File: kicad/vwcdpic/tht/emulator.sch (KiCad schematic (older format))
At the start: 33 parts, among them P1 CONN_9, P2 CONN_3, Q1 IRF7343PBF, U1 PIC12F629, U2 78L05, U3 TL072

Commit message: tht separated board for emulator, separated board for audio
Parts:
- removed C6, C7: 10m, symbol C
- removed C8: 47m, symbol C
- removed Q1: IRF7343PBF, SO8, symbol IRF7343PBF
- removed R10, R11: 10k, symbol R
- removed R18: 10, symbol R
- added C10, C11, C12, C13, C14, C16, C18, C6: 100m, symbol CAPAPOL
- added C15, C17: 100n, symbol C
- added C7, C8: 10m, symbol CAPAPOL
- added P3: Aout, symbol CONN_4
- added R19, R20: 100, symbol R
- added RV1, RV2: 100k, symbol POT
- added U4: TL071, symbol TL071
- C4: value C -> 1m
- C5: value 2m2 -> 100n
- C9: value 47m -> 100n
- P1: value CONN_9 -> digi; symbol CONN_9 -> CONN_7
- P2: value CONN_3 -> Ain
- R14, R15: value 330k -> 2k2
- R16, R17: value 7M5 -> 22k
- R2: value 1M -> 22k
- R3: value 1k -> 22k
- R4: value 1k5 -> 10
- R8, R9: value 10k -> 100k
- U2: footprint (none) -> to92
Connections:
- net +12V: now also R4.2, C17.1, C18.1, P3.4 (P4); no longer P1.4 (P4), R3.2, R8.2, U3.8 (V+), U3.8 (V+)
- net AGND: now also C5.2, C9.2, R3.2, R8.1, R9.1, U3.4 (V-), U3.4 (V-), C10.2, C11.2, C12.2, C15.2, C16.2, C17.2, C18.2, C6.2, P3.2 (P2), RV1.1, RV2.1, U4.4 (V-); no longer P1.2 (P2)
- net CLK: now also P1.3 (P3); no longer P1.9 (P9)
- net DataIn: now also P1.5 (P5); no longer P1.8 (P8)
- net GND: now also P1.2 (P2), P1.4 (P4); no longer C5.1, R2.1, R9.1, U3.4 (V-), U3.4 (V-)
- net POWER_CTL: now also C2.1, P1.1 (P1), U2.VI; no longer P1.5 (P5), R2.2
- net left_in: now also RV2.2
- net left_out: now also P3.1 (P1), R20.1; no longer C9.2, P1.1 (P1)
- net right_in: now also RV1.2
- net right_out: now also P3.3 (P3), R19.1; no longer P1.3 (P3)
- net at U1.2 (GP5/OSC1): now also R1.1, U1.3 (GP4/OSC2), U1.4 (GP3/MCLR)
- net filtered_12V: now reaches R4.1
- net filtered_12V: now also C5.1, R2.1, U3.8 (V+), U3.8 (V+), C6.1, U4.7 (V+)
- net at R3.1: now also C9.1, R2.2, C10.1, U4.3 (+); no longer R4.2
- net at R16.2, U3.1: now also C13.1
- net at R12.1, U3.3 (+): now also C7.1
- net at R13.2, U3.5 (+): now also C8.1
- net at R17.1, U3.6 (-): now also R15.2; no longer R15.1
- net at R17.2, U3.7: now also C14.1; no longer C9.1
- new net: C12.1, R14.2
- new net: C11.1, R15.1
- new net: C13.2, R19.2, R8.2
- new net: C14.2, R20.2, R9.2
- new net: C8.2, RV2.3
- new net: C7.2, RV1.3
- new net +6V: C15.1, C16.1, R12.2, R13.1, U4.2 (-), U4.6
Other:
- moved on the sheet: C1, C2, C3, C4, P2, R1, R12, R13, R14, R16, R17, U2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

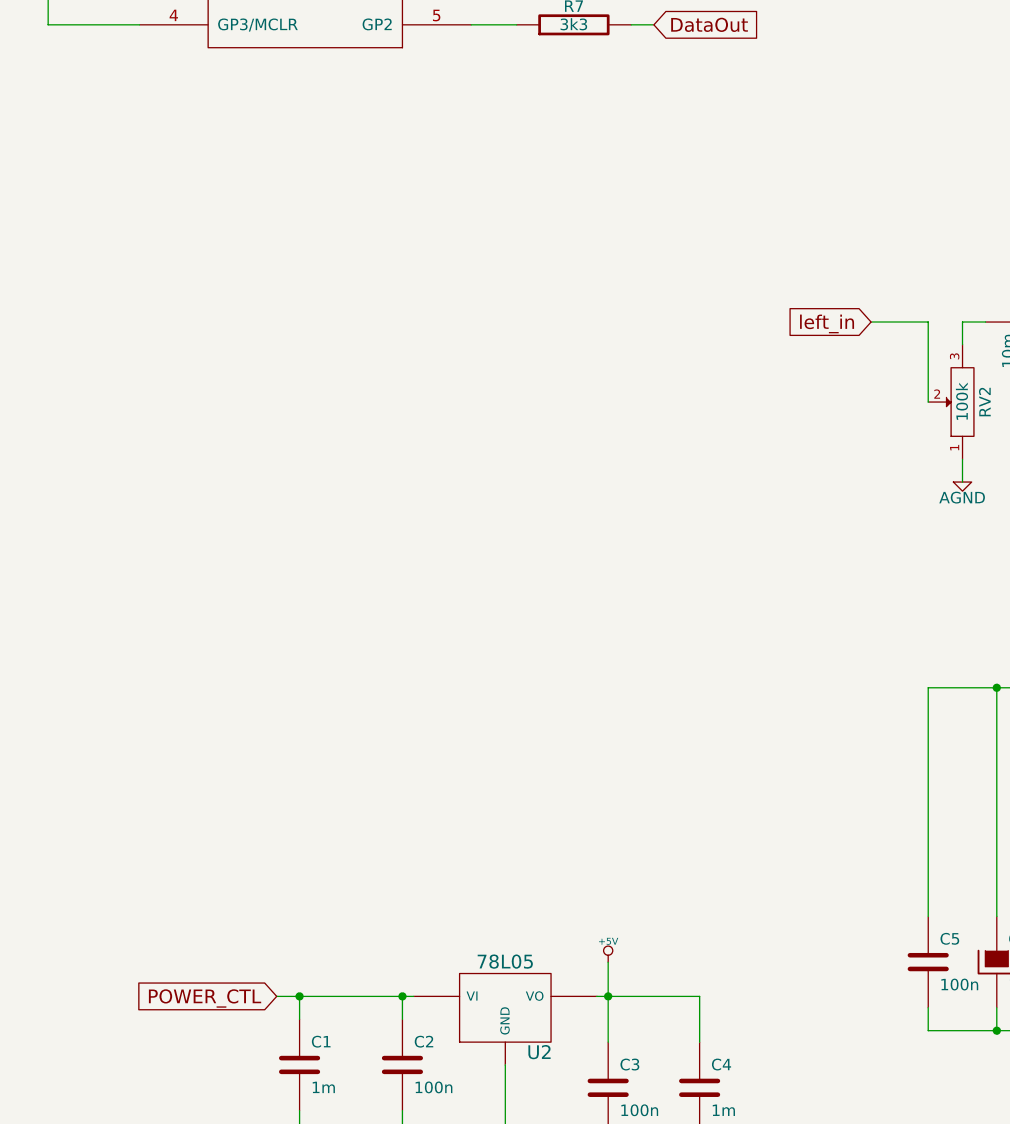
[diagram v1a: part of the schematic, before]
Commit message: kicad module for BLK-MD-SPK-B.mod http://www.elecfreaks.com/store/audio-bluetooth-speaker-module-blkmdspkb-p-541.html
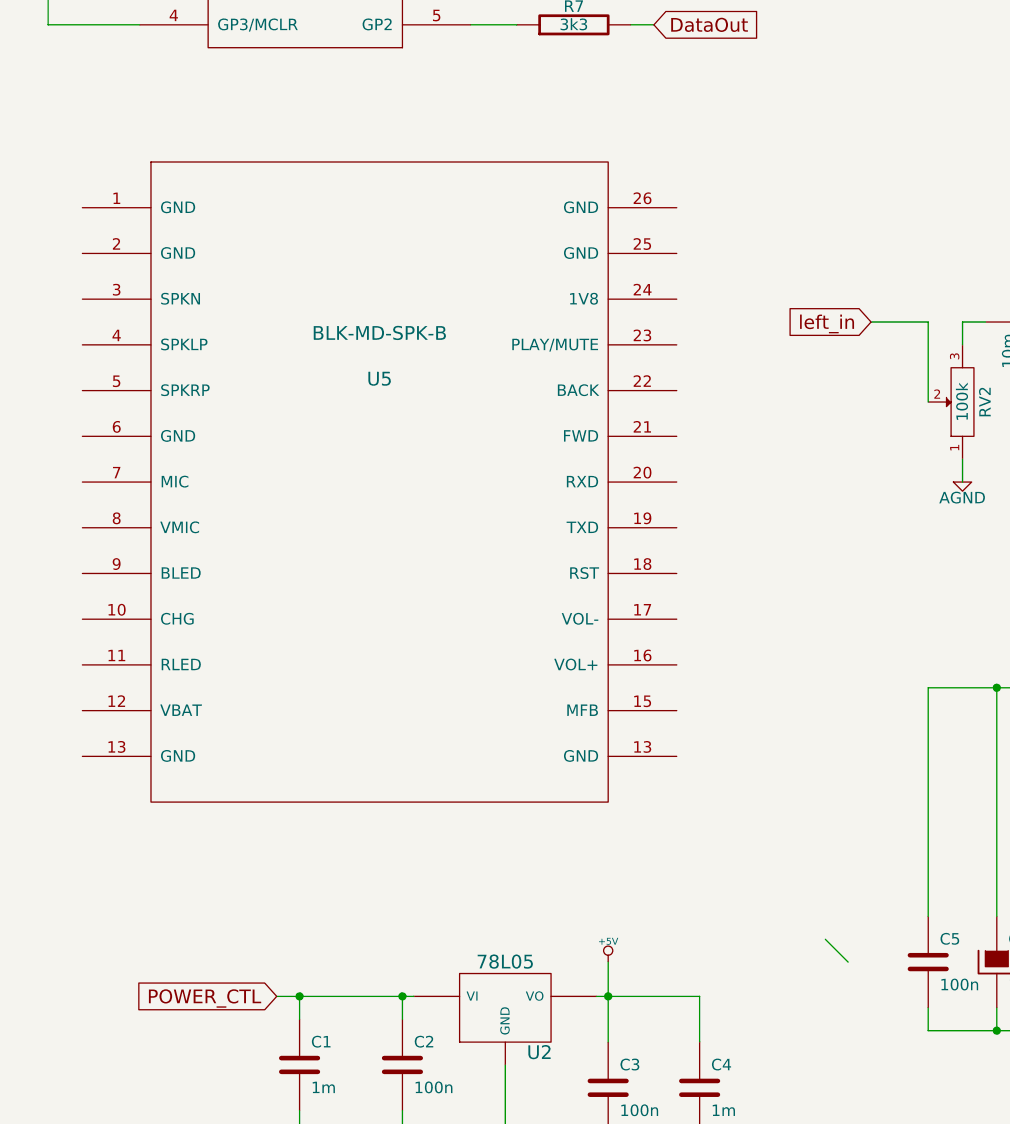
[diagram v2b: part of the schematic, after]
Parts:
- added U5: BLK-MD-SPK-B, ~, symbol BLK-MD-SPK-B

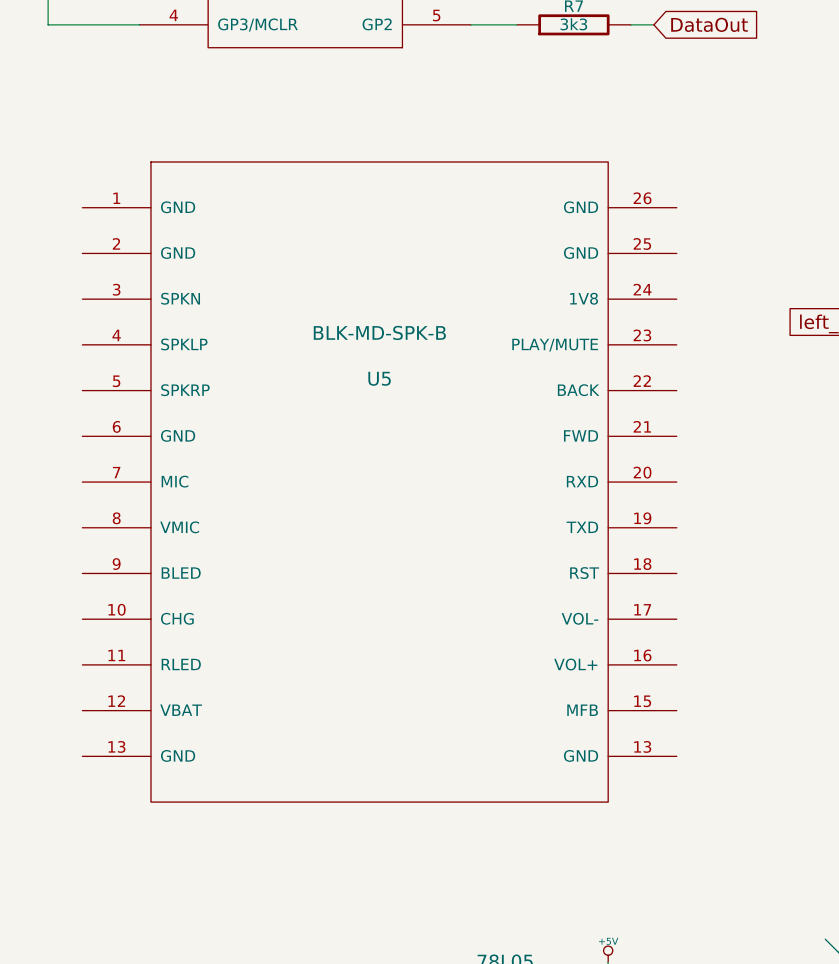
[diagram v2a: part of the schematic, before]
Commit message: change audio board to 5x5cm
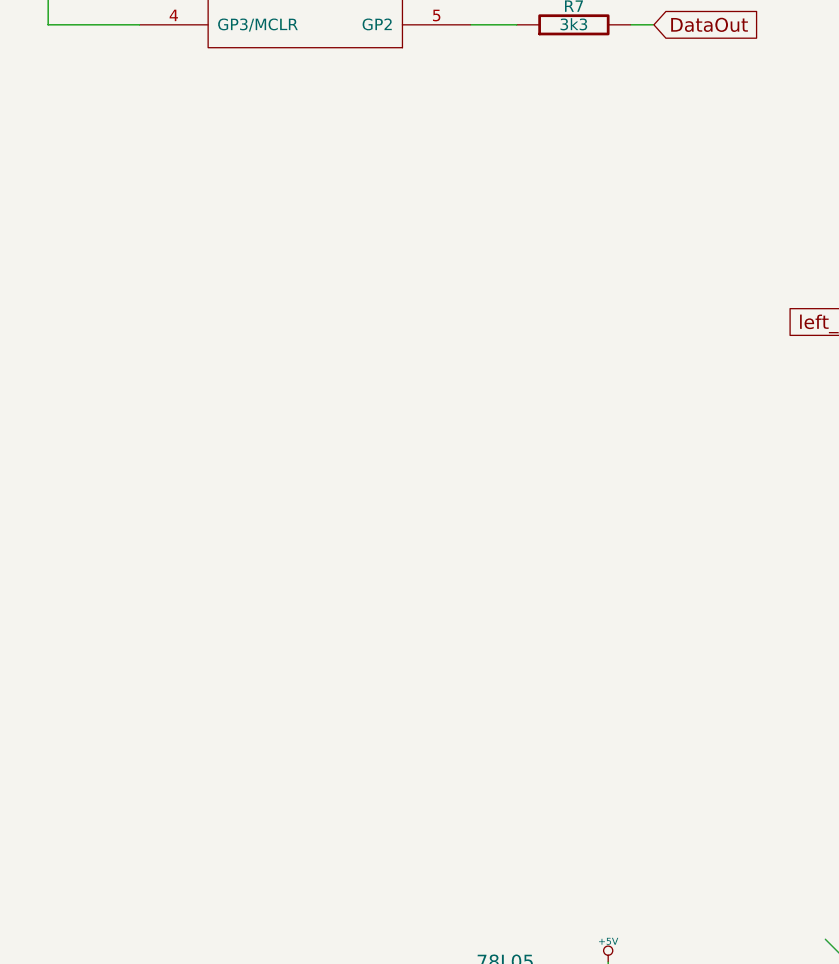
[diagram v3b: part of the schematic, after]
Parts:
- removed U5: BLK-MD-SPK-B, ~, symbol BLK-MD-SPK-B
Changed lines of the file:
@@
 LIBS:contrib
 LIBS:valves
-LIBS:BLK-MD-SPK-B
 LIBS:emulator-cache
-EELAYER 27 0
+EELAYER 24 0
 EELAYER END
 $Descr A4 11693 8268
@@
 	1    0    0    -1
 $EndComp
-$Comp
-L BLK-MD-SPK-B U5
-U 1 1 541FF883
-P 2800 3900
-F 0 "U5" H 2800 3800 60  0000 C CNN
-F 1 "BLK-MD-SPK-B" H 2800 4000 60  0000 C CNN
-F 2 "~" H 2800 3900 60  0000 C CNN
-F 3 "~" H 2800 3900 60  0000 C CNN
-	1    2800 3900
-	1    0    0    -1
-$EndComp

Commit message: ..
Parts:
- U2: footprint to92 -> (none)
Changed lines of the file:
@@
 LIBS:contrib
 LIBS:valves
+LIBS:aimtec
+LIBS:BLK-MD-SPK-B
 LIBS:emulator-cache
-EELAYER 24 0
+EELAYER 25 0
 EELAYER END
 $Descr A4 11693 8268
@@
 filtered_12V
 $Comp
-L AGND #PWR01
+L AGND #PWR10
 U 1 1 53B6BBA5
 P 7250 2850
-F 0 "#PWR01" H 7250 2850 40  0001 C CNN
+F 0 "#PWR10" H 7250 2850 40  0001 C CNN
 F 1 "AGND" H 7250 2780 50  0000 C CNN
 F 2 "" H 7250 2850 60  0001 C CNN
@@
 $EndComp
 $Comp
-L AGND #PWR02
+L AGND #PWR11
 U 1 1 53B6B685
 P 7400 6900
-F 0 "#PWR02" H 7400 6900 40  0001 C CNN
+F 0 "#PWR11" H 7400 6900 40  0001 C CNN
 F 1 "AGND" H 7400 6830 50  0000 C CNN
 F 2 "" H 7400 6900 60  0001 C CNN
@@
 $EndComp
 $Comp
-L AGND #PWR03
+L AGND #PWR9
 U 1 1 53B6B682
 P 7050 4550
-F 0 "#PWR03" H 7050 4550 40  0001 C CNN
+F 0 "#PWR9" H 7050 4550 40  0001 C CNN
 F 1 "AGND" H 7050 4480 50  0000 C CNN
 F 2 "" H 7050 4550 60  0001 C CNN
@@
 $EndComp
 $Comp
-L AGND #PWR04
+L AGND #PWR13
 U 1 1 53B6B665
 P 8100 4350
-F 0 "#PWR04" H 8100 4350 40  0001 C CNN
+F 0 "#PWR13" H 8100 4350 40  0001 C CNN
 F 1 "AGND" H 8100 4280 50  0000 C CNN
 F 2 "" H 8100 4350 60  0001 C CNN
@@
 $EndComp
 $Comp
-L AGND #PWR05
+L AGND #PWR8
 U 1 1 53B6B661
 P 6900 3200
-F 0 "#PWR05" H 6900 3200 40  0001 C CNN
+F 0 "#PWR8" H 6900 3200 40  0001 C CNN
 F 1 "AGND" H 6900 3130 50  0000 C CNN
 F 2 "" H 6900 3200 60  0001 C CNN
@@
 $EndComp
 $Comp
-L AGND #PWR06
+L AGND #PWR6
 U 1 1 53B6B65C
 P 5350 4450
-F 0 "#PWR06" H 5350 4450 40  0001 C CNN
+F 0 "#PWR6" H 5350 4450 40  0001 C CNN
 F 1 "AGND" H 5350 4380 50  0000 C CNN
 F 2 "" H 5350 4450 60  0001 C CNN
@@
 $EndComp
 $Comp
-L AGND #PWR07
+L AGND #PWR5
 U 1 1 53B6B64D
 P 5350 1900
-F 0 "#PWR07" H 5350 1900 40  0001 C CNN
+F 0 "#PWR5" H 5350 1900 40  0001 C CNN
 F 1 "AGND" H 5350 1830 50  0000 C CNN
 F 2 "" H 5350 1900 60  0001 C CNN
@@
 $EndComp
 $Comp
-L AGND #PWR08
+L AGND #PWR7
 U 1 1 53B6B646
 P 6900 1750
-F 0 "#PWR08" H 6900 1750 40  0001 C CNN
+F 0 "#PWR7" H 6900 1750 40  0001 C CNN
 F 1 "AGND" H 6900 1680 50  0000 C CNN
 F 2 "" H 6900 1750 60  0001 C CNN
@@
 $EndComp
 $Comp
-L AGND #PWR09
+L AGND #PWR12
 U 1 1 53B6B5FF
 P 8100 1950
-F 0 "#PWR09" H 8100 1950 40  0001 C CNN
+F 0 "#PWR12" H 8100 1950 40  0001 C CNN
 F 1 "AGND" H 8100 1880 50  0000 C CNN
 F 2 "" H 8100 1950 60  0001 C CNN
@@
 $EndComp
 $Comp
-L AGND #PWR010
+L AGND #PWR18
 U 1 1 52E56AD2
 P 9700 2700
-F 0 "#PWR010" H 9700 2700 40  0001 C CNN
+F 0 "#PWR18" H 9700 2700 40  0001 C CNN
 F 1 "AGND" H 9700 2630 50  0000 C CNN
 F 2 "" H 9700 2700 60  0001 C CNN
@@
 $EndComp
 $Comp
-L +12V #PWR011
+L +12V #PWR14
 U 1 1 53B69937
 P 9050 5250
-F 0 "#PWR011" H 9050 5200 20  0001 C CNN
+F 0 "#PWR14" H 9050 5200 20  0001 C CNN
 F 1 "+12V" H 9050 5350 30  0000 C CNN
 F 2 "" H 9050 5250 60  0001 C CNN
@@
 $EndComp
 $Comp
-L +5V #PWR012
+L +5V #PWR4
 U 1 1 52D02FCA
 P 3800 6550
-F 0 "#PWR012" H 3800 6640 20  0001 C CNN
+F 0 "#PWR4" H 3800 6640 20  0001 C CNN
 F 1 "+5V" H 3800 6640 30  0000 C CNN
 F 2 "" H 3800 6550 60  0001 C CNN
@@
 $EndComp
 $Comp
-L GND #PWR013
+L GND #PWR3
 U 1 1 52D02FA3
 P 3350 7600
-F 0 "#PWR013" H 3350 7600 30  0001 C CNN
+F 0 "#PWR3" H 3350 7600 30  0001 C CNN
 F 1 "GND" H 3350 7530 30  0001 C CNN
 F 2 "" H 3350 7600 60  0001 C CNN
@@
 $EndComp
 $Comp
-L AGND #PWR014
+L AGND #PWR17
 U 1 1 52E56ACB
 P 9700 2300
-F 0 "#PWR014" H 9700 2300 40  0001 C CNN
+F 0 "#PWR17" H 9700 2300 40  0001 C CNN
 F 1 "AGND" H 9700 2230 50  0000 C CNN
 F 2 "" H 9700 2300 60  0001 C CNN
@@
 POWER_CTL
 $Comp
-L +12V #PWR015
+L +12V #PWR15
 U 1 1 52D3D406
 P 9450 2750
-F 0 "#PWR015" H 9450 2700 20  0001 C CNN
+F 0 "#PWR15" H 9450 2700 20  0001 C CNN
 F 1 "+12V" H 9450 2850 30  0000 C CNN
 F 2 "" H 9450 2750 60  0001 C CNN
@@
 $EndComp
 $Comp
-L GND #PWR016
+L GND #PWR16
 U 1 1 52D3D3F9
 P 9700 1300
-F 0 "#PWR016" H 9700 1300 30  0001 C CNN
+F 0 "#PWR16" H 9700 1300 30  0001 C CNN
 F 1 "GND" H 9700 1230 30  0001 C CNN
 F 2 "" H 9700 1300 60  0001 C CNN
@@
 $EndComp
 $Comp
-L +5V #PWR017
+L +5V #PWR1
 U 1 1 52D03030
 P 1750 850
-F 0 "#PWR017" H 1750 940 20  0001 C CNN
+F 0 "#PWR1" H 1750 940 20  0001 C CNN
 F 1 "+5V" H 1750 940 30  0000 C CNN
 F 2 "" H 1750 850 60  0001 C CNN
@@
 $EndComp
 $Comp
-L GND #PWR018
+L GND #PWR2
 U 1 1 52D02FB7
 P 3200 1550
-F 0 "#PWR018" H 3200 1550 30  0001 C CNN
+F 0 "#PWR2" H 3200 1550 30  0001 C CNN
 F 1 "GND" H 3200 1480 30  0001 C CNN
 F 2 "" H 3200 1550 60  0001 C CNN
@@
 $Comp
 L 78L05 U2
-U 1 1 52D02F38
+U 1 1 548091CF
 P 3350 6750
 F 0 "U2" H 3500 6554 60  0000 C CNN
 F 1 "78L05" H 3350 6950 60  0000 C CNN
-F 2 "to92" H 3350 6750 60  0001 C CNN
-F 3 "" H 3350 6750 60  0001 C CNN
+F 2 "" H 3350 6750 60  0000 C CNN
+F 3 "" H 3350 6750 60  0000 C CNN
 	1    3350 6750
 	1    0    0    -1
 $EndComp
-Entry Wire Line
-	4750 6450 4850 6550
 $EndSCHEMATC
